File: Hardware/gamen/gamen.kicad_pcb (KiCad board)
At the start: 2 copper layers, 1 part, among them U1 STM32H743IGTx

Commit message: GAMEN: Started SDRAM
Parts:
- added C12: 100nF, Capacitor_SMD:C_0402_1005Metric_Pad0.74x0.62mm_HandSolder, F.Cu at (178.7, 120.8)
- added C33: 100nF, Capacitor_SMD:C_0402_1005Metric_Pad0.74x0.62mm_HandSolder, F.Cu at (178.7, 122.8)
- added J2: Conn_01x05_Pin, Connector_Molex:Molex_PicoBlade_53048-0510_1x05_P1.25mm_Horizontal, F.Cu at (141.4, 118.0)
- added J3: UART_Header, MyFootprints:CONN04_530480410_MOL, F.Cu at (153.7, 117.8)
- added R10: 100Ω, Resistor_SMD:R_0402_1005Metric_Pad0.72x0.64mm_HandSolder, F.Cu at (178.7, 116.9)
- added R14: 100Ω, Resistor_SMD:R_0402_1005Metric_Pad0.72x0.64mm_HandSolder, F.Cu at (178.7, 118.8)
- added RST1: SW_Push, Button_Switch_SMD:SW_SPST_B3U-1000P, F.Cu at (162.8, 122.8)
- added SW1: SW_SPDT, Connector_PinHeader_2.54mm:PinHeader_1x03_P2.54mm_Vertical, F.Cu at (169.6, 113.6)
- added TP6: TP_UARTTX, TestPoint:TestPoint_Pad_D1.0mm, F.Cu at (178.7, 112.8)
- added U14: ~, Package_TO_SOT_SMD:SOT-23-3, F.Cu at (174.5, 118.1)
- added U2: STM32H743IITx, Package_QFP:LQFP-176_24x24mm_P0.5mm, F.Cu at (153.1, 101.8)
- added U3: AS4C16M16SA-6TIN, Package_SO:TSOP-II-54_22.2x10.16mm_P0.8mm, B.Cu at (153.1, 101.8)
- added Y1: 25MHz, Crystal:Crystal_SMD_WE_CFPX-180-4Pin_3.2x2.5mm, F.Cu at (174.5, 113.6)
- U1: value STM32H743IGTx -> TPS562201DDCR; footprint Package_QFP:LQFP-176_24x24mm_P0.5mm -> Package_TO_SOT_SMD:SOT-23-6
- moved U1 22.1 mm to (162.4, 118.4)
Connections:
- U1 pad 1: unconnected-(U1-PE2-Pad1) -> GND
- U1 pad 2: unconnected-(U1-PE3-Pad2) -> Net-(U1-SW)
- U1 pad 3: unconnected-(U1-PE4-Pad3) -> +5V
- U1 pad 4: unconnected-(U1-PE5-Pad4) -> Net-(U1-VFB)
- U1 pad 5: unconnected-(U1-PE6-Pad5) -> +5V
- U1 pad 6: unconnected-(U1-VBAT-Pad6) -> Net-(U1-VBST)
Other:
- copper layers 2 -> 6

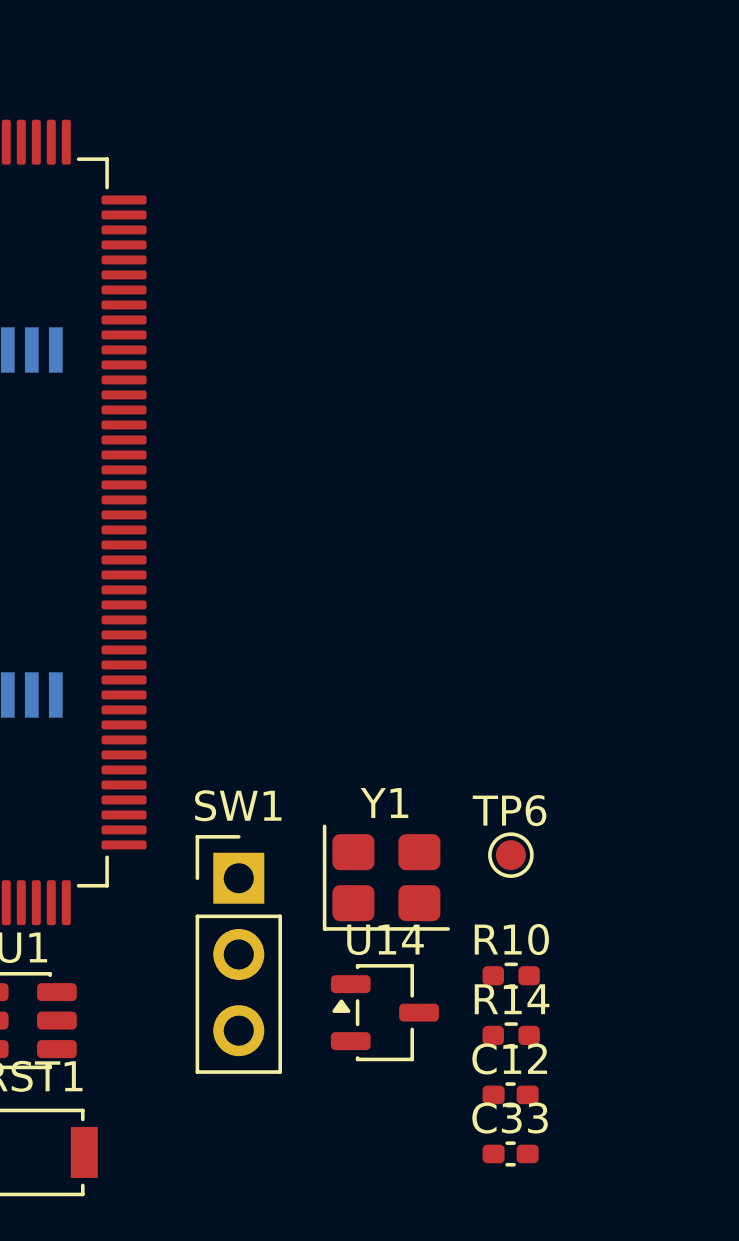
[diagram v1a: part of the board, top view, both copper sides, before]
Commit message: Gamen: Screen connected to mcu
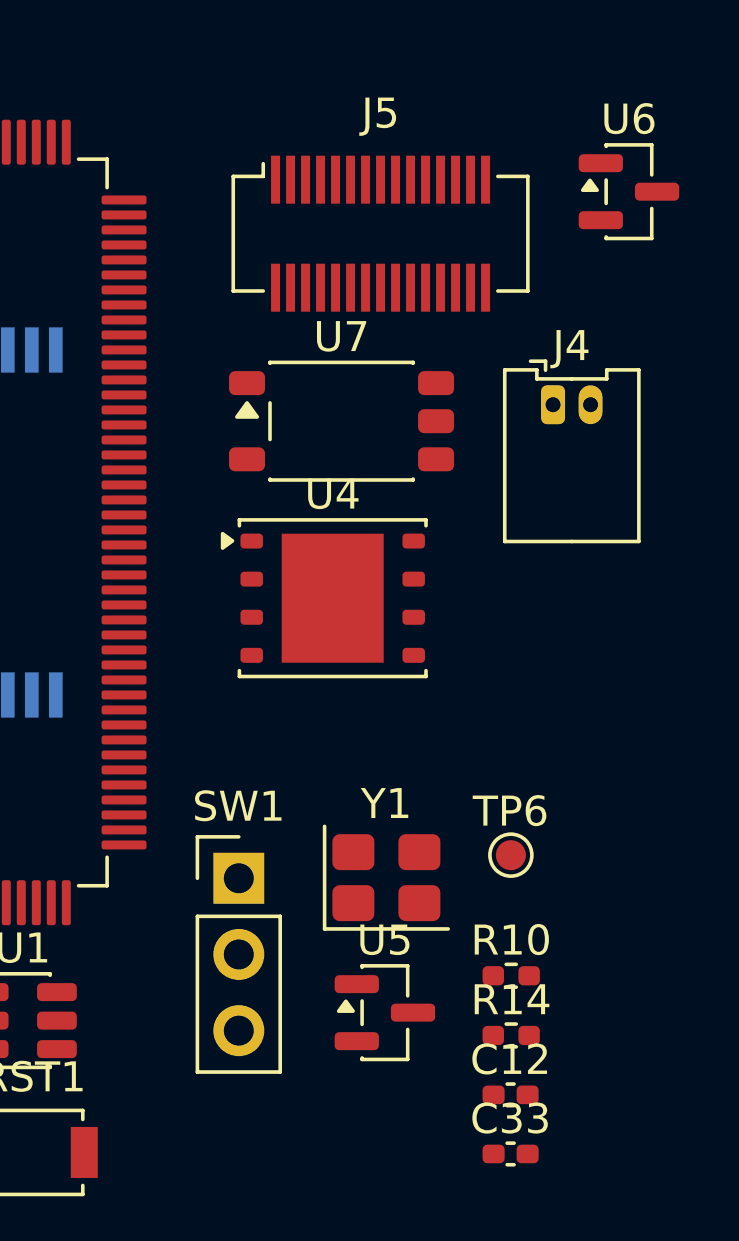
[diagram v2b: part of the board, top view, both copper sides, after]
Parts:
- added J4: MIDI CONN, Connector_Molex:Molex_PicoBlade_53048-0210_1x02_P1.25mm_Horizontal, F.Cu at (180.1, 97.8)
- added J5: SCREEN CONN, Connector_Hirose:Hirose_DF12_DF12C3.0-30DS-0.5V_2x15_P0.50mm_Vertical, F.Cu at (174.3, 92.1)
- added U4: W25Q256JWPIQ, Package_SON:WSON-8-1EP_6x5mm_P1.27mm_EP3.4x4.3mm, F.Cu at (172.7, 104.3)
- added U6: ~, Package_TO_SOT_SMD:SOT-23, F.Cu at (182.6, 90.7)
- added U7: TLP2361(E, Package_SO:SO-5-6_4.55x3.7mm_P1.27mm, F.Cu at (173.0, 98.4)
- U5: renamed from U14; footprint Package_TO_SOT_SMD:SOT-23-3 -> Package_TO_SOT_SMD:SOT-23
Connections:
- J3 pad 2: /UART_RX -> /UART_TX
- J3 pad 3: /UART_TX -> /UART_RX
- U2 pad 104: unconnected-(U2-PD14-Pad104) -> /SDRAM_DQ0
- U2 pad 105: unconnected-(U2-PD15-Pad105) -> /SDRAM_DQ1
- U2 pad 106: unconnected-(U2-PG2-Pad106) -> /SDRAM_A12
- U2 pad 108: unconnected-(U2-PG4-Pad108) -> /SDRAM_BA0
- U2 pad 109: unconnected-(U2-PG5-Pad109) -> /SDRAM_BA1
- U2 pad 112: unconnected-(U2-PG8-Pad112) -> /SDRAM_CLK
- U2 pad 142: unconnected-(U2-PD0-Pad142) -> /SDRAM_DQ0
- U2 pad 143: unconnected-(U2-PD1-Pad143) -> /SDRAM_DQ3
- U2 pad 16: unconnected-(U2-PF0-Pad16) -> /SDRAM_A0
- U2 pad 160: unconnected-(U2-PG15-Pad160) -> /SDRAM_CAS
- U2 pad 169: unconnected-(U2-PE0-Pad169) -> /SDRAM_NBL0
- U2 pad 17: unconnected-(U2-PF1-Pad17) -> /SDRAM_A1
- U2 pad 170: unconnected-(U2-PE1-Pad170) -> /SDRAM_NBL1
- U2 pad 18: unconnected-(U2-PF2-Pad18) -> /SDRAM_A2
- U2 pad 19: unconnected-(U2-PF3-Pad19) -> /SDRAM_A3
- U2 pad 20: unconnected-(U2-PF4-Pad20) -> /SDRAM_A4
- U2 pad 21: unconnected-(U2-PF5-Pad21) -> /SDRAM_A5
- U2 pad 24: unconnected-(U2-PF6-Pad24) -> /QSPI_IO3
- U2 pad 25: unconnected-(U2-PF7-Pad25) -> /QSPI_IO2
- U2 pad 26: unconnected-(U2-PF8-Pad26) -> /QSPI_IO1
- U2 pad 27: unconnected-(U2-PF9-Pad27) -> /QSPI_IO0
- U2 pad 28: unconnected-(U2-PF10-Pad28) -> /QSPI_CLK
- U2 pad 32: unconnected-(U2-PC0-Pad32) -> /SDRAM_WE
- U2 pad 34: unconnected-(U2-PC2_C-Pad34) -> /SDRAM_CS
- U2 pad 35: unconnected-(U2-PC3_C-Pad35) -> /SDRAM_CKE
- U2 pad 40: unconnected-(U2-PA0-Pad40) -> Net-(U2-PA0)
- U2 pad 59: unconnected-(U2-PF11-Pad59) -> /SDNIS_RAS
- U2 pad 60: unconnected-(U2-PF12-Pad60) -> /SDRAM_A6
- U2 pad 63: unconnected-(U2-PF13-Pad63) -> /SDRAM_A7
- U2 pad 64: unconnected-(U2-PF14-Pad64) -> /SDRAM_A8
- U2 pad 65: unconnected-(U2-PF15-Pad65) -> /SDRAM_A9
- U2 pad 66: unconnected-(U2-PG0-Pad66) -> /SDRAM_A10
- U2 pad 67: unconnected-(U2-PG1-Pad67) -> /SDRAM_A11
- U2 pad 68: unconnected-(U2-PE7-Pad68) -> /SDRAM_DQ6
- U2 pad 69: unconnected-(U2-PE8-Pad69) -> /SDRAM_DQ5
- U2 pad 70: unconnected-(U2-PE9-Pad70) -> /SDRAM_DQ4
- U2 pad 73: unconnected-(U2-PE10-Pad73) -> /SDRAM_DQ7
- U2 pad 74: unconnected-(U2-PE11-Pad74) -> /SDRAM_DQ8
- U2 pad 75: unconnected-(U2-PE12-Pad75) -> /SDRAM_DQ9
- U2 pad 76: unconnected-(U2-PE13-Pad76) -> /SDRAM_DQ10
- U2 pad 77: unconnected-(U2-PE14-Pad77) -> /SDRAM_DQ11
- U2 pad 78: unconnected-(U2-PE15-Pad78) -> /SDRAM_DQ12
- U2 pad 92: unconnected-(U2-PB12-Pad92) -> /UART_TX
- U2 pad 93: unconnected-(U2-PB13-Pad93) -> /UART_RX
- U2 pad 96: unconnected-(U2-PD8-Pad96) -> /SDRAM_DQ13
- U2 pad 97: unconnected-(U2-PD9-Pad97) -> /SDRAM_DQ14
- U2 pad 98: unconnected-(U2-PD10-Pad98) -> /SDRAM_DQ15
- U3 pad 10: unconnected-(U3-DQ5-Pad10) -> /SDRAM_DQ5
- U3 pad 11: unconnected-(U3-DQ6-Pad11) -> /SDRAM_DQ6
- U3 pad 12: unconnected-(U3-VSSQ-Pad12) -> GND
- U3 pad 13: unconnected-(U3-DQ7-Pad13) -> /SDRAM_DQ7
- U3 pad 14: unconnected-(U3-VDD-Pad14) -> +3.3V
- U3 pad 15: unconnected-(U3-LDQM-Pad15) -> /SDRAM_NBL0
- U3 pad 16: unconnected-(U3-*WE-Pad16) -> /SDRAM_WE
- U3 pad 17: unconnected-(U3-*CAS-Pad17) -> /SDRAM_CAS
- U3 pad 18: unconnected-(U3-*RAS-Pad18) -> /SDNIS_RAS
- U3 pad 19: unconnected-(U3-*CS-Pad19) -> /SDRAM_CS
- U3 pad 2: unconnected-(U3-DQ0-Pad2) -> /SDRAM_DQ0
- U3 pad 20: unconnected-(U3-BA0-Pad20) -> /SDRAM_BA0
- U3 pad 21: unconnected-(U3-BA1-Pad21) -> /SDRAM_BA1
- U3 pad 22: unconnected-(U3-A10/AP-Pad22) -> /SDRAM_A10
- U3 pad 23: unconnected-(U3-A0-Pad23) -> /SDRAM_A0
- U3 pad 24: unconnected-(U3-A1-Pad24) -> /SDRAM_A1
- U3 pad 25: unconnected-(U3-A2-Pad25) -> /SDRAM_A2
- U3 pad 26: unconnected-(U3-A3-Pad26) -> /SDRAM_A3
- U3 pad 28: unconnected-(U3-VSS-Pad28) -> GND
- U3 pad 29: unconnected-(U3-A4-Pad29) -> /SDRAM_A4
- U3 pad 3: unconnected-(U3-VDDQ-Pad3) -> +3.3V
- U3 pad 30: unconnected-(U3-A5-Pad30) -> /SDRAM_A5
- U3 pad 31: unconnected-(U3-A6-Pad31) -> /SDRAM_A6
- U3 pad 32: unconnected-(U3-A7-Pad32) -> /SDRAM_A7
- U3 pad 33: unconnected-(U3-A8-Pad33) -> /SDRAM_A8
- U3 pad 34: unconnected-(U3-A9-Pad34) -> /SDRAM_A9
- U3 pad 35: unconnected-(U3-A11-Pad35) -> /SDRAM_A11
- U3 pad 36: unconnected-(U3-A12-Pad36) -> /SDRAM_A12
- U3 pad 37: unconnected-(U3-CKE-Pad37) -> /SDRAM_CKE
- U3 pad 38: unconnected-(U3-CLK-Pad38) -> /SDRAM_CLK
- U3 pad 39: unconnected-(U3-UDQM-Pad39) -> /SDRAM_NBL1
- U3 pad 4: unconnected-(U3-DQ1-Pad4) -> /SDRAM_DQ1
- U3 pad 41: unconnected-(U3-VSS-Pad41) -> GND
- U3 pad 42: unconnected-(U3-DQ8-Pad42) -> /SDRAM_DQ8
- U3 pad 43: unconnected-(U3-VDDQ-Pad43) -> +3.3V
- U3 pad 44: unconnected-(U3-DQ9-Pad44) -> /SDRAM_DQ9
- U3 pad 45: unconnected-(U3-DQ10-Pad45) -> /SDRAM_DQ10
- U3 pad 46: unconnected-(U3-VSSQ-Pad46) -> GND
- U3 pad 47: unconnected-(U3-DQ11-Pad47) -> /SDRAM_DQ11
- U3 pad 48: unconnected-(U3-DQ12-Pad48) -> /SDRAM_DQ12
- U3 pad 49: unconnected-(U3-VDDQ-Pad49) -> +3.3V
- U3 pad 5: unconnected-(U3-DQ2-Pad5) -> /SDRAM_DQ2
- U3 pad 50: unconnected-(U3-DQ13-Pad50) -> /SDRAM_DQ13
- U3 pad 51: unconnected-(U3-DQ14-Pad51) -> /SDRAM_DQ14
- U3 pad 52: unconnected-(U3-VSSQ-Pad52) -> GND
- U3 pad 53: unconnected-(U3-DQ15-Pad53) -> /SDRAM_DQ15
- U3 pad 54: unconnected-(U3-VSS-Pad54) -> GND
- U3 pad 6: unconnected-(U3-VSSQ-Pad6) -> GND
- U3 pad 7: unconnected-(U3-DQ3-Pad7) -> /SDRAM_DQ3
- U3 pad 8: unconnected-(U3-DQ4-Pad8) -> /SDRAM_DQ4
- U3 pad 9: unconnected-(U3-VDDQ-Pad9) -> +3.3V
- U5 pad 1: unconnected-(U14-IO1-Pad1) -> /UART_TX
- U5 pad 2: /UART_RX_RES -> /UART_RX
